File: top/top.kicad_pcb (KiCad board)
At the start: 4 copper layers, 28.3 x 40 mm, 23 parts, among them P1 CONN_10, P2 CONN_5, P3 CONN_20, U1 IQS572, U4 ESD

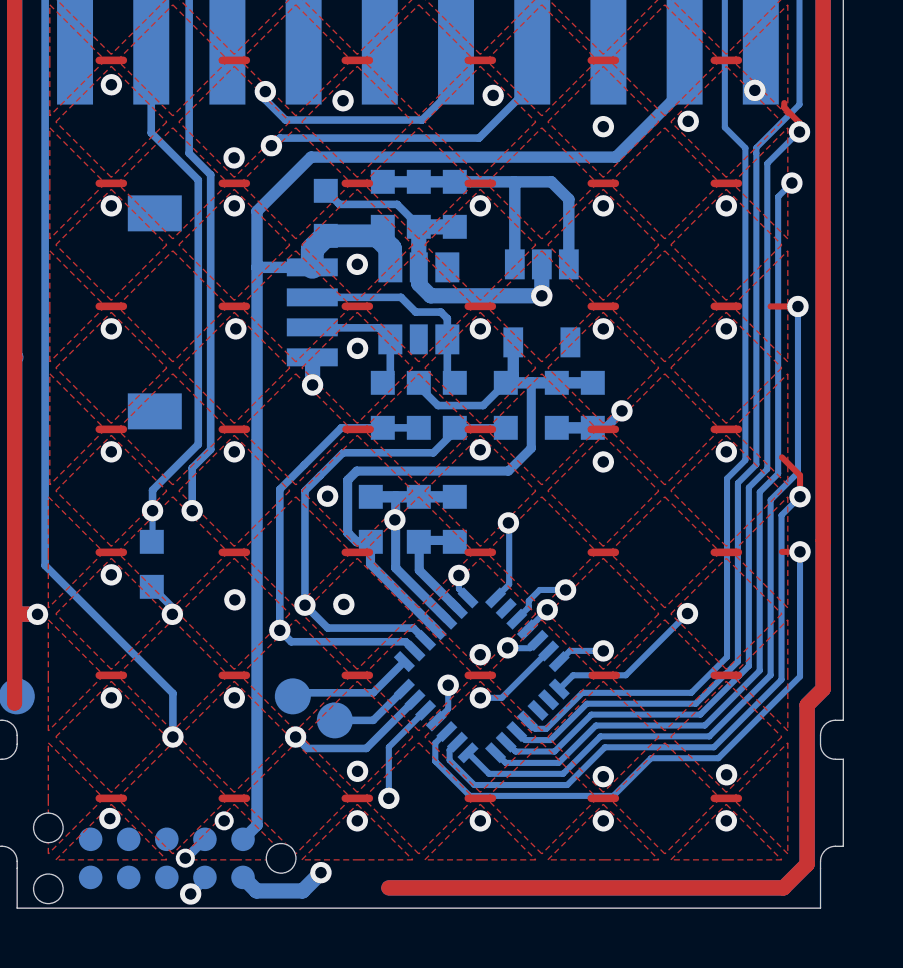
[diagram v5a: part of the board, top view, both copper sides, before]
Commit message: Fix DRC errors.
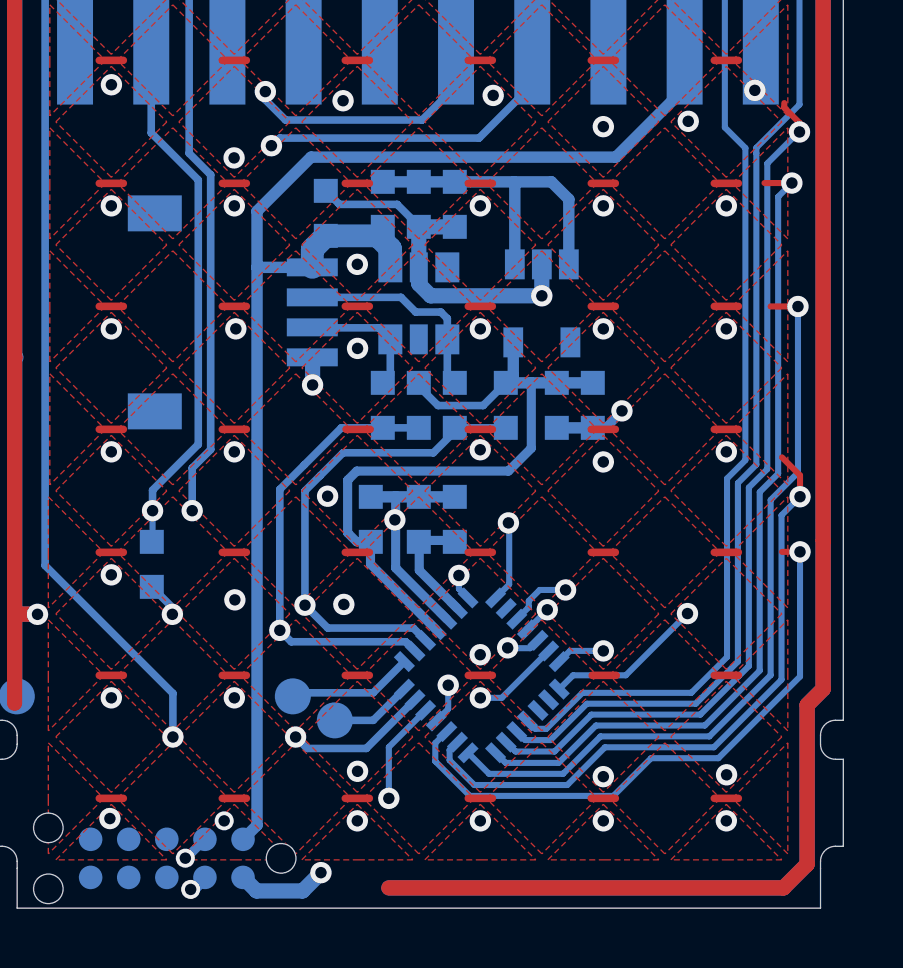
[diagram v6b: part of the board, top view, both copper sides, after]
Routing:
- net /TX3: track 31.7 -> 32.6 mm
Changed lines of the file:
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@@
     (thickness 1.6)
     (drawings 74)
-    (tracks 523)
+    (tracks 524)
     (zones 0)
     (modules 23)
@@
   )
   (setup
-    (last_trace_width 0.254)
+    (last_trace_width 0.2032)
     (user_trace_width 0.2032)
     (user_trace_width 0.254)
@@
   (segment (start 204.178679 152.2) (end 202.9 152.2) (width 0.254) (layer B.Cu) (net 7))
   (segment (start 205.21906 151.159619) (end 204.178679 152.2) (width 0.254) (layer B.Cu) (net 7))
-  (via (at 198.0946 157.988) (size 0.7112) (drill 0.381) (layers F.Cu B.Cu) (net 8))
+  (via (at 198.0946 157.8356) (size 0.635) (drill 0.381) (layers F.Cu B.Cu) (net 8))
   (segment (start 208.6 142.45) (end 206.9 142.45) (width 0.254) (layer B.Cu) (net 8))
   (via (at 201.9046 148.3614) (size 0.7112) (drill 0.381) (layers F.Cu B.Cu) (net 8))
   (segment (start 198.57 157.5126) (end 198.0946 157.988) (width 0.3048) (layer B.Cu) (net 8))
   (segment (start 198.57 157.435) (end 198.57 157.5126) (width 0.3048) (layer B.Cu) (net 8))
-  (segment (start 198.0946 157.988) (end 198.755 157.988) (width 0.254) (layer In2.Cu) (net 8))
   (segment (start 206.9 142.566602) (end 206.9 142.45) (width 0.254) (layer B.Cu) (net 8))
   (segment (start 206.185202 143.2814) (end 206.9 142.566602) (width 0.254) (layer B.Cu) (net 8))
@@
   (segment (start 201.9046 144.5514) (end 201.9046 148.3614) (width 0.254) (layer B.Cu) (net 8))
   (segment (start 202.4126 144.0434) (end 201.9046 144.5514) (width 0.254) (layer B.Cu) (net 8))
-  (segment (start 200.7108 155.982698) (end 200.8378 155.855698) (width 0.254) (layer In2.Cu) (net 8))
-  (segment (start 200.7108 156.0322) (end 200.7108 155.982698) (width 0.254) (layer In2.Cu) (net 8))
-  (segment (start 198.755 157.988) (end 200.7108 156.0322) (width 0.254) (layer In2.Cu) (net 8))
-  (segment (start 200.8378 155.855698) (end 200.8378 150.7744) (width 0.254) (layer In2.Cu) (net 8))
-  (segment (start 201.9046 149.7076) (end 201.9046 148.3614) (width 0.254) (layer In2.Cu) (net 8))
-  (segment (start 200.8378 150.7744) (end 201.9046 149.7076) (width 0.254) (layer In2.Cu) (net 8))
   (segment (start 202.6666 149.1234) (end 201.9046 148.3614) (width 0.254) (layer B.Cu) (net 8))
   (segment (start 205.926167 149.533274) (end 205.516293 149.1234) (width 0.254) (layer B.Cu) (net 8))
@@
   (segment (start 201.9046 148.3614) (end 201.48041 147.93721) (width 0.254) (layer In2.Cu) (net 8))
   (segment (start 201.48041 147.93721) (end 201.48041 134.51079) (width 0.254) (layer In2.Cu) (net 8))
+  (segment (start 201.9046 149.7076) (end 201.9046 148.3614) (width 0.254) (layer In2.Cu) (net 8))
+  (segment (start 198.0946 157.861) (end 198.882 157.861) (width 0.254) (layer In2.Cu) (net 8))
+  (segment (start 200.7108 156.0322) (end 200.7108 155.982698) (width 0.254) (layer In2.Cu) (net 8))
+  (segment (start 200.7108 155.982698) (end 200.8378 155.855698) (width 0.254) (layer In2.Cu) (net 8))
+  (segment (start 198.882 157.861) (end 200.7108 156.0322) (width 0.254) (layer In2.Cu) (net 8))
+  (segment (start 200.8378 155.855698) (end 200.8378 150.7744) (width 0.254) (layer In2.Cu) (net 8))
+  (segment (start 200.8378 150.7744) (end 201.9046 149.7076) (width 0.254) (layer In2.Cu) (net 8))
   (segment (start 208.9 134.2748) (end 208.9 137) (width 0.381) (layer B.Cu) (net 9))
   (segment (start 204.5 134.25) (end 208.8752 134.25) (width 0.381) (layer B.Cu) (net 9))
@@
   (segment (start 215.55 122) (end 216.35 122) (width 0.254) (layer F.Cu) (net 22))
   (via (at 218.313 123.6218) (size 0.7112) (drill 0.381) (layers F.Cu B.Cu) (net 22))
-  (segment (start 216.5858 122.0978) (end 216.6874 121.9962) (width 0.2032) (layer B.Cu) (net 40))
   (segment (start 218.313 123.6218) (end 218.0844 123.6218) (width 0.2032) (layer F.Cu) (net 22))
   (segment (start 218.0844 123.6218) (end 217.6526 123.19) (width 0.2032) (layer F.Cu) (net 22))
@@
   (segment (start 215.233738 152.372033) (end 217.063366 150.542405) (width 0.2032) (layer B.Cu) (net 25))
   (segment (start 208.259619 153.28094) (end 208.597871 153.619199) (width 0.2032) (layer B.Cu) (net 25))
+  (segment (start 218.1352 134.2898) (end 217.2208 134.2898) (width 0.2032) (layer F.Cu) (net 25))
   (segment (start 205.572614 151.513173) (end 203.949187 153.1366) (width 0.254) (layer B.Cu) (net 31))
   (segment (start 203.949187 153.1366) (end 201.9808 153.1366) (width 0.254) (layer B.Cu) (net 31))
@@
   (segment (start 204.7 153.092893) (end 204.7 154.8) (width 0.2032) (layer B.Cu) (net 36))
   (via (at 204.7 154.8) (size 0.7112) (drill 0.381) (layers F.Cu B.Cu) (net 36))
+  (segment (start 216.5858 122.0978) (end 216.6874 121.9962) (width 0.2032) (layer B.Cu) (net 40))
   (zone (net 1) (net_name GND) (layer In1.Cu) (hatch edge 0.508)
     (connect_pads (clearance 0.254))

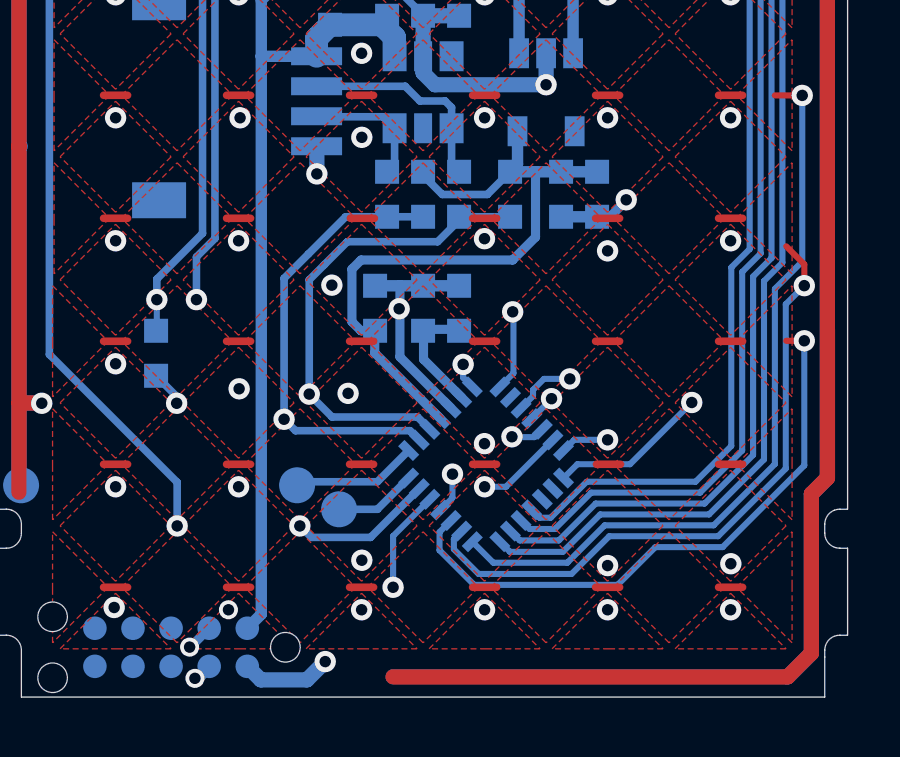
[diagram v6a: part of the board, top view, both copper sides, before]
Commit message: Fix DRC errors.
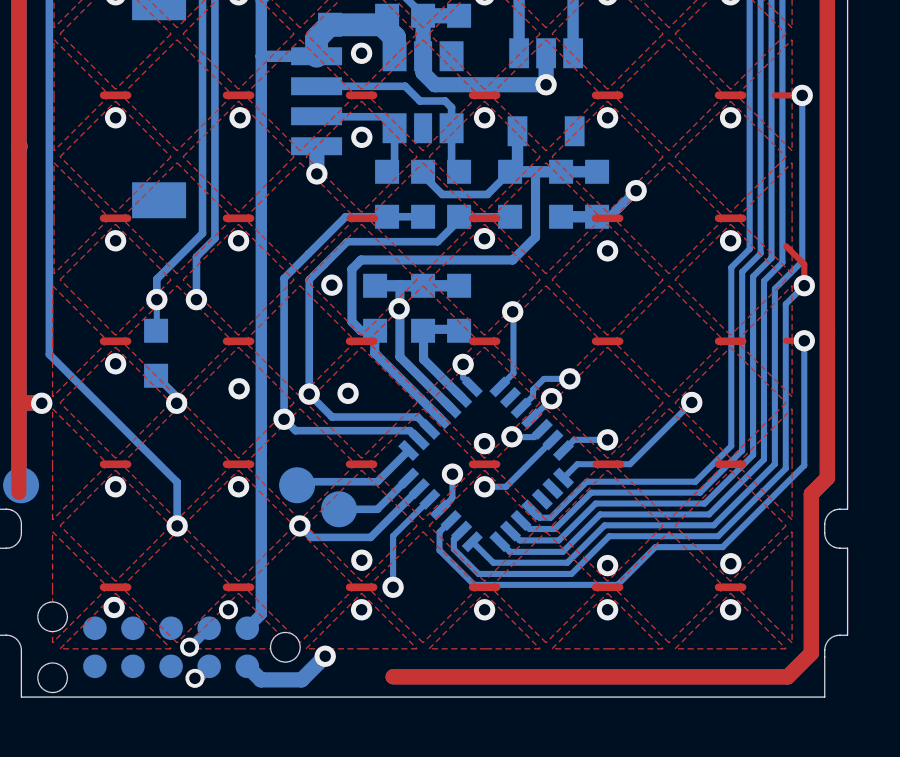
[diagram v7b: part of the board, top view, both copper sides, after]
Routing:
- net GND: track 248.1 -> 248.6 mm
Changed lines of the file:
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@@
-(kicad_pcb (version 20171130) (host pcbnew "(5.0.0)")
+(kicad_pcb (version 20171130) (host pcbnew "(5.1.5)-2")
   (general
     (thickness 1.6)
     (drawings 74)
-    (tracks 524)
+    (tracks 523)
     (zones 0)
     (modules 23)
@@
     (zone_45_only no)
     (trace_min 0.2032)
-    (segment_width 0.254)
-    (edge_width 0.1)
     (via_size 0.7112)
     (via_drill 0.381)
@@
     (uvia_min_size 0.508)
     (uvia_min_drill 0.127)
+    (edge_width 0.1)
+    (segment_width 0.254)
     (pcb_text_width 0.3)
     (pcb_text_size 1.5 1.5)
@@
     (uvia_dia 0.7112)
     (uvia_drill 0.381)
+    (diff_pair_width 0.254)
     (diff_pair_gap 0.254)
-    (diff_pair_width 0.254)
     (add_net +3V3)
     (add_net +5V)
@@
   (gr_arc (start 219.589762 152.99753) (end 219.089772 152.997519) (angle -90) (layer Edge.Cuts) (width 0.01))
   (via (at 216.9 131.2) (size 0.7112) (drill 0.381) (layers F.Cu B.Cu) (net 1))
-  (via (at 202.438 157.2768) (size 0.7112) (drill 0.381) (layers F.Cu B.Cu) (net 1))
   (via (at 202.1586 141.0208) (size 0.7112) (drill 0.381) (layers F.Cu B.Cu) (net 1))
   (segment (start 192.2272 151.638) (end 192.2272 122.05119) (width 0.508) (layer B.Cu) (net 1))
@@
   (segment (start 209.8 138.049) (end 209.8 137) (width 0.508) (layer B.Cu) (net 1))
   (via (at 209.8 138.049) (size 0.7112) (drill 0.381) (layers F.Cu B.Cu) (net 1))
-  (segment (start 199.84 157.435) (end 200.2914 157.8864) (width 0.508) (layer B.Cu) (net 1))
-  (segment (start 201.8284 157.8864) (end 202.438 157.2768) (width 0.508) (layer B.Cu) (net 1))
-  (segment (start 200.2914 157.8864) (end 201.8284 157.8864) (width 0.508) (layer B.Cu) (net 1))
   (segment (start 217.8558 157.7848) (end 218.6432 156.9974) (width 0.508) (layer B.Cu) (net 1))
   (segment (start 218.6432 151.6888) (end 218.6432 156.9974) (width 0.508) (layer F.Cu) (net 1))
@@
   (segment (start 204.9272 144.7546) (end 204.9018 144.7292) (width 0.3048) (layer B.Cu) (net 1))
   (segment (start 204.9272 145.288) (end 204.9272 144.7546) (width 0.3048) (layer B.Cu) (net 1))
-  (via (at 212.471 141.8844) (size 0.7112) (drill 0.381) (layers F.Cu B.Cu) (net 1))
-  (segment (start 212.471 141.9098) (end 212.471 141.8844) (width 0.3048) (layer B.Cu) (net 1))
-  (segment (start 211.5 142.45) (end 211.9308 142.45) (width 0.3048) (layer B.Cu) (net 1))
-  (segment (start 211.9308 142.45) (end 212.471 141.9098) (width 0.3048) (layer B.Cu) (net 1))
+  (via (at 212.8012 141.5796) (size 0.7112) (drill 0.381) (layers F.Cu B.Cu) (net 1))
   (segment (start 192.2272 121.412) (end 192.2272 122.0724) (width 0.508) (layer B.Cu) (net 1))
   (segment (start 194.4878 119.1514) (end 192.2272 121.412) (width 0.508) (layer B.Cu) (net 1))
@@
   (segment (start 202.6 134.55) (end 203.051 135.001) (width 0.254) (layer B.Cu) (net 1))
   (segment (start 203.051 135.001) (end 204.978 135.001) (width 0.254) (layer B.Cu) (net 1))
+  (segment (start 211.9308 142.45) (end 212.8012 141.5796) (width 0.3048) (layer B.Cu) (net 1))
+  (segment (start 211.5 142.45) (end 211.9308 142.45) (width 0.3048) (layer B.Cu) (net 1))
+  (segment (start 201.6506 157.8864) (end 202.438 157.099) (width 0.508) (layer B.Cu) (net 1))
+  (via (at 202.438 157.099) (size 0.7112) (drill 0.381) (layers F.Cu B.Cu) (net 1))
+  (segment (start 200.2914 157.8864) (end 201.6506 157.8864) (width 0.508) (layer B.Cu) (net 1))
+  (segment (start 199.84 157.435) (end 200.2914 157.8864) (width 0.508) (layer B.Cu) (net 1))
   (segment (start 206.65 140.7) (end 206.9 140.95) (width 0.254) (layer B.Cu) (net 2))
   (segment (start 206.65 139.5) (end 206.65 140.7) (width 0.254) (layer B.Cu) (net 2))

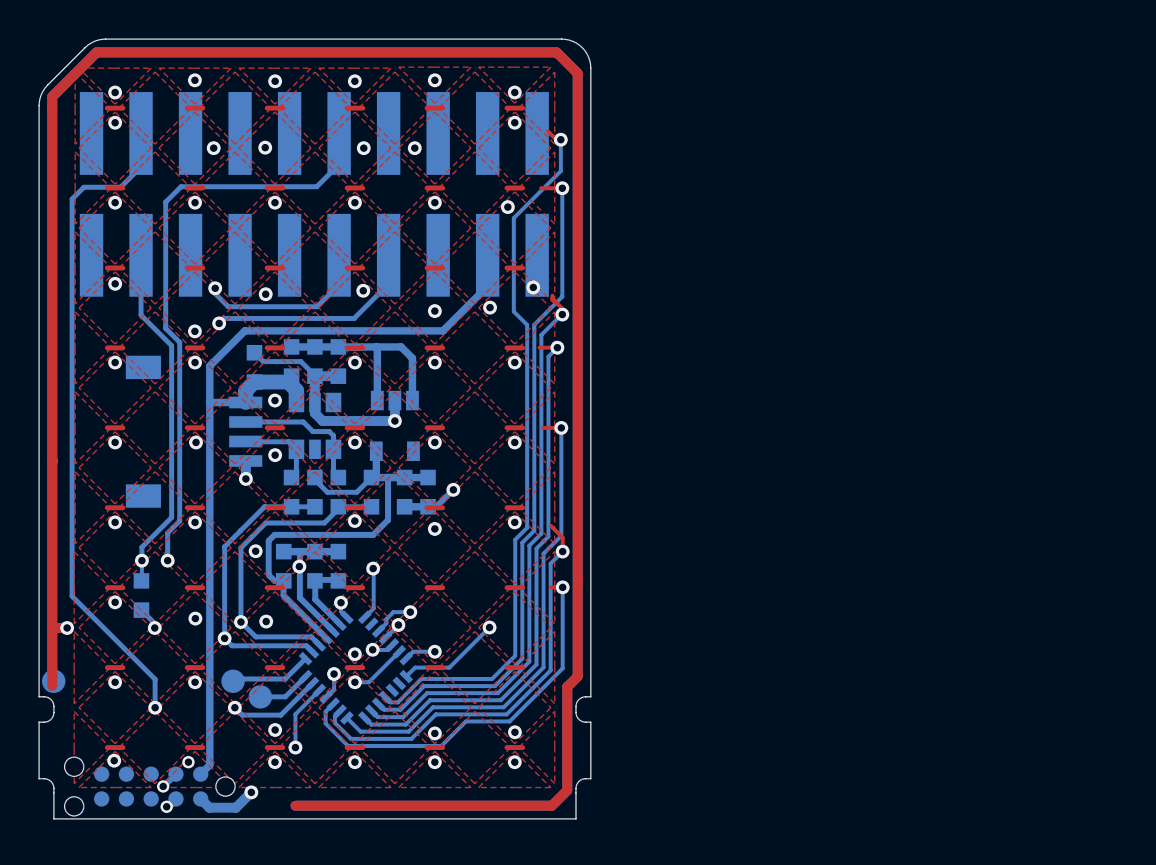
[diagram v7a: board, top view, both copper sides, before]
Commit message: Improved GND layer. (Add zone array to swapped inner layer.)
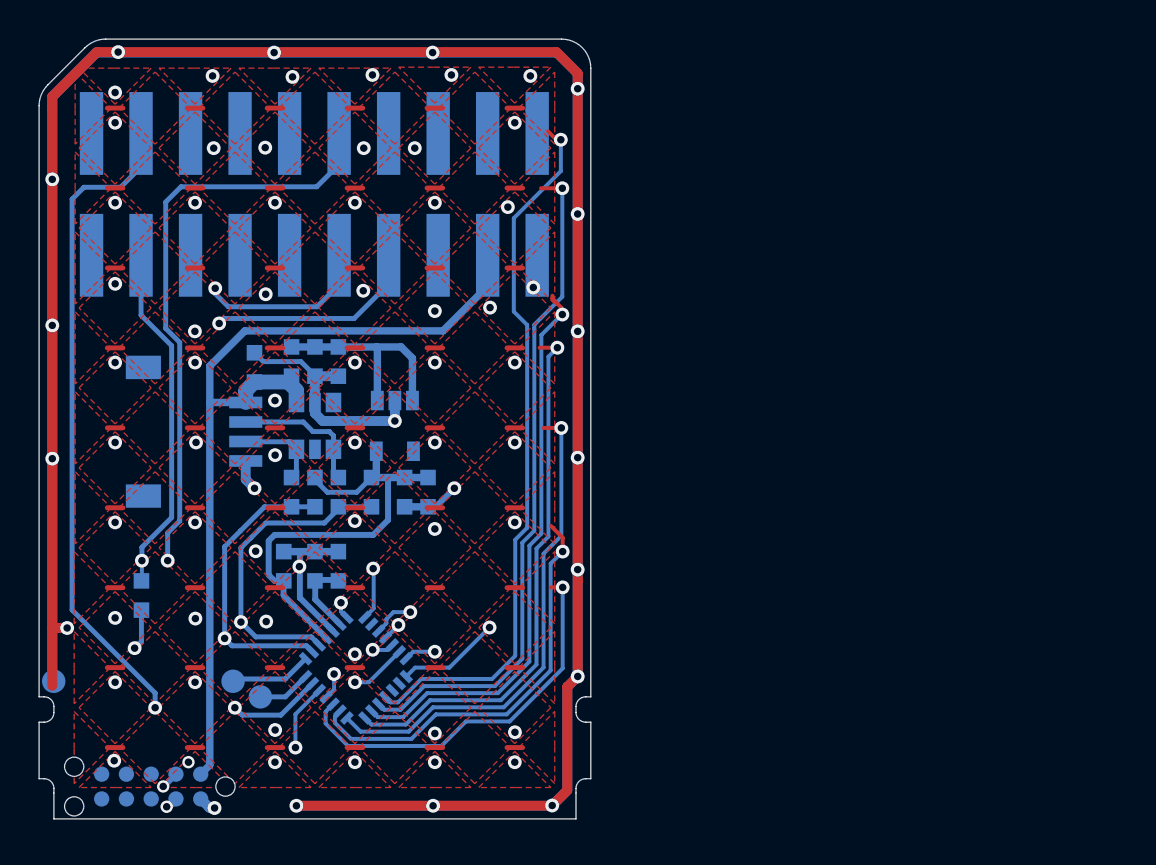
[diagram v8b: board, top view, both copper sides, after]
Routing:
- net GND: track 248.6 -> 430.5 mm, vias 8 -> 23
- net /RX2: track 45.1 -> 46.9 mm
- net /RX3: track 38.9 -> 40.5 mm
- net /RX5: track 42.6 -> 43.8 mm
- net /SCL: track 55.0 -> 56.0 mm
- net /RX4: track 37.8 -> 38.4 mm
- net /RX1: track 48.1 -> 48.6 mm
- added copper zone on In2.Cu, net GND
- removed copper zone on In1.Cu, net GND
